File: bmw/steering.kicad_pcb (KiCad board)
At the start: 2 copper layers, 16 parts, among them P1 CONN_01X03, P2 CONN_01X12, P3 CONN_01X03, P4 CONN_01X12, U1 ProMicro, U2 TH3122, U3 MCP41100, U4 4053

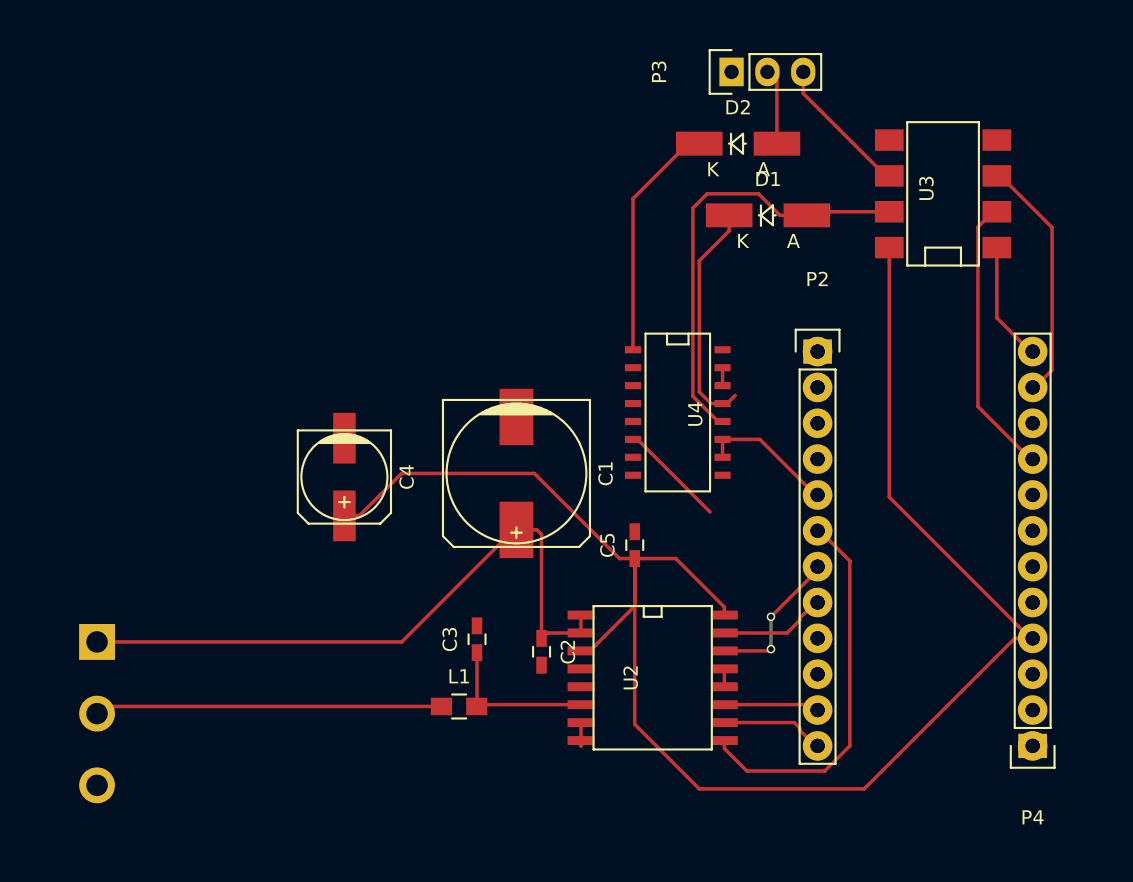
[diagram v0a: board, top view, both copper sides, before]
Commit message: Wersja 0.1 plytki PCB. Nie dodano slotow na zasilanie z przetwornicy.
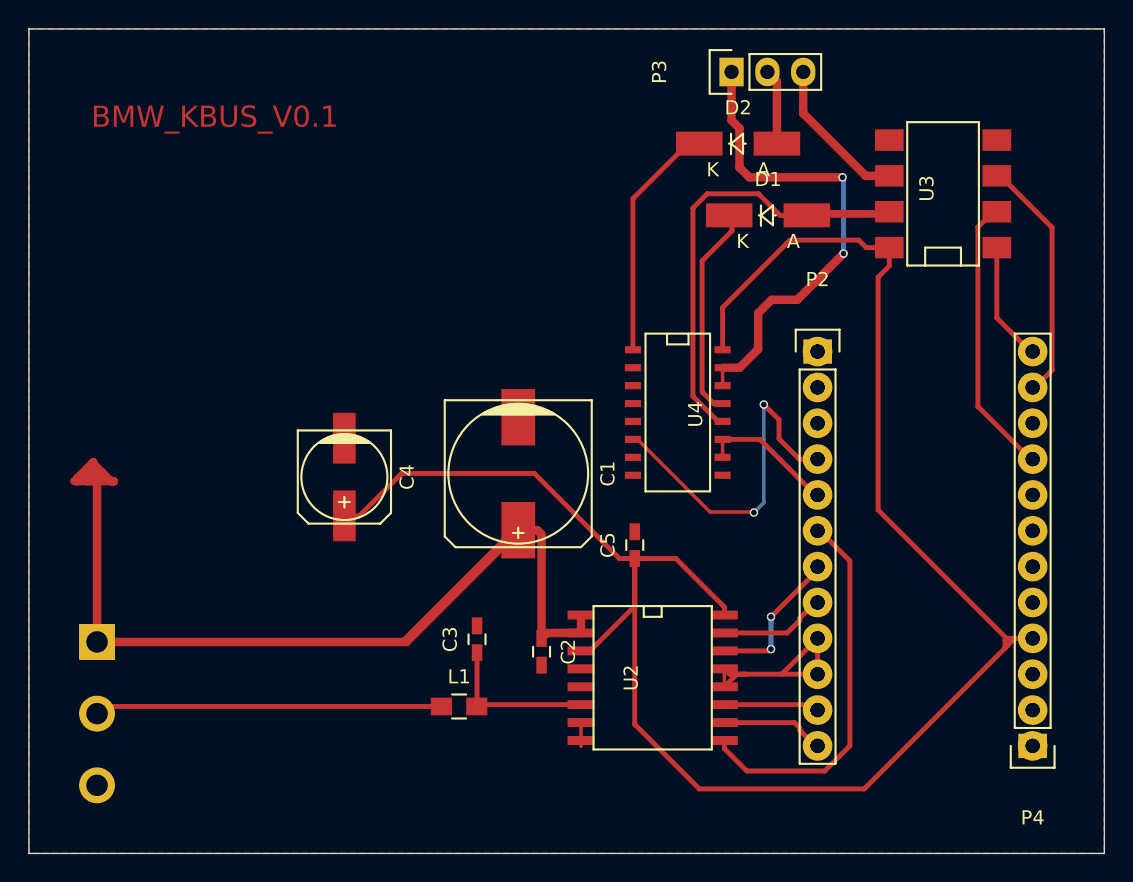
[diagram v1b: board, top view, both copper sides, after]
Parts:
- moved C1 0.13 mm to (154.1, 79.8)
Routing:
- net /SLEEVE_: track 1.59 -> 63.0 mm, vias 0 -> 2
- net +12V: track 46.5 -> 103.6 mm
- net +5V: track 119.7 -> 139.3 mm
- net /MUX_EN: track 7.59 -> 24.9 mm, vias 0 -> 2
- net Earth: track 1.27 -> 16.1 mm
- net /PB0: track 31.2 -> 37.2 mm
- net /RING: track 5.36 -> 10.7 mm
- net /TIP: track 10.0 -> 11.1 mm
- net Net-(D1-Pad1): track 16.5 -> 15.7 mm
- added copper zone on F.Cu, net Earth
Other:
- board outline added: 76.2 x 58.4 mm
- net class 12v added: clearance 0.2, trace_width 0.6, via_dia 0.6, via_drill 0.4
- net class Default: trace_width 0.25 -> 0.35
- board text added: "BMW_KBUS_V0.1"

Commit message: Zrezygnowano z przetwornicy na rzecz LDO LM1117 5V. Pozostało połączyć masę układu w dwóch punktach. Poprawnie przechodzi testy DRC. Można wykonać prototyp.
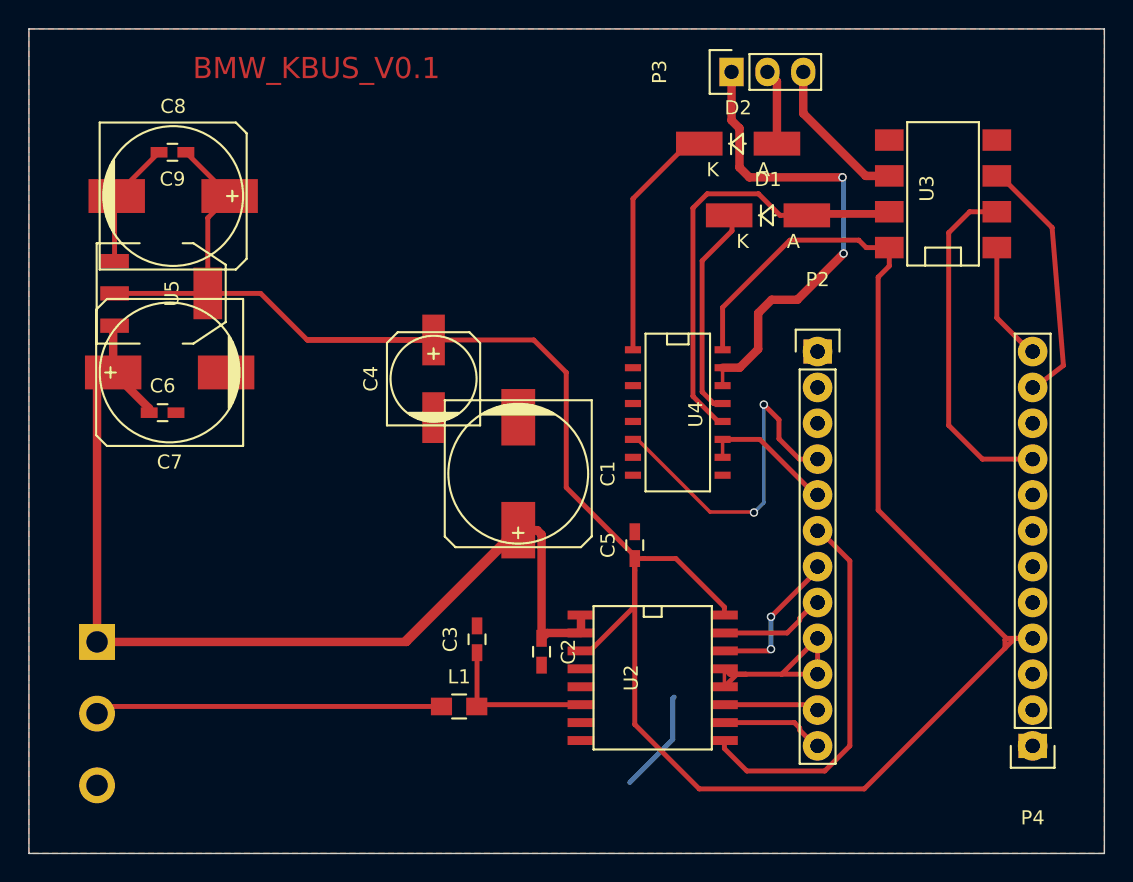
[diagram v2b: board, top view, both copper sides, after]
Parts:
- added C6: 100n, Capacitors_SMD:C_0603_HandSoldering, F.Cu at (128.8, 75.5)
- added C7: 100u, Capacitors_SMD:c_elec_10x10, F.Cu at (129.3, 72.6)
- added C8: 100u, Capacitors_SMD:c_elec_10x10, F.Cu at (129.6, 60.1)
- added C9: 100n, Capacitors_SMD:C_0603_HandSoldering, F.Cu at (129.6, 57.0)
- added U5: LM1117-5.0, TO_SOT_Packages_SMD:SOT-223, F.Cu at (128.8, 67.0)
- moved C4 9.40 mm to (148.1, 73.0), turned to 90 degrees
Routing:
- net +5V: track 139.3 -> 185.3 mm
- net Earth: track 16.1 -> 25.1 mm
- net (no net): track 0.00 -> 7.35 mm
- net +12V: track 103.6 -> 110.6 mm
- net /SCLK: track 19.9 -> 25.0 mm
- net Net-(U2-Pad7): track 1.65 -> 0.00 mm
- net /MOSI: track 17.4 -> 17.9 mm
